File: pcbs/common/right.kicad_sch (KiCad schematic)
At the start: 89 parts, among them J2 TRS

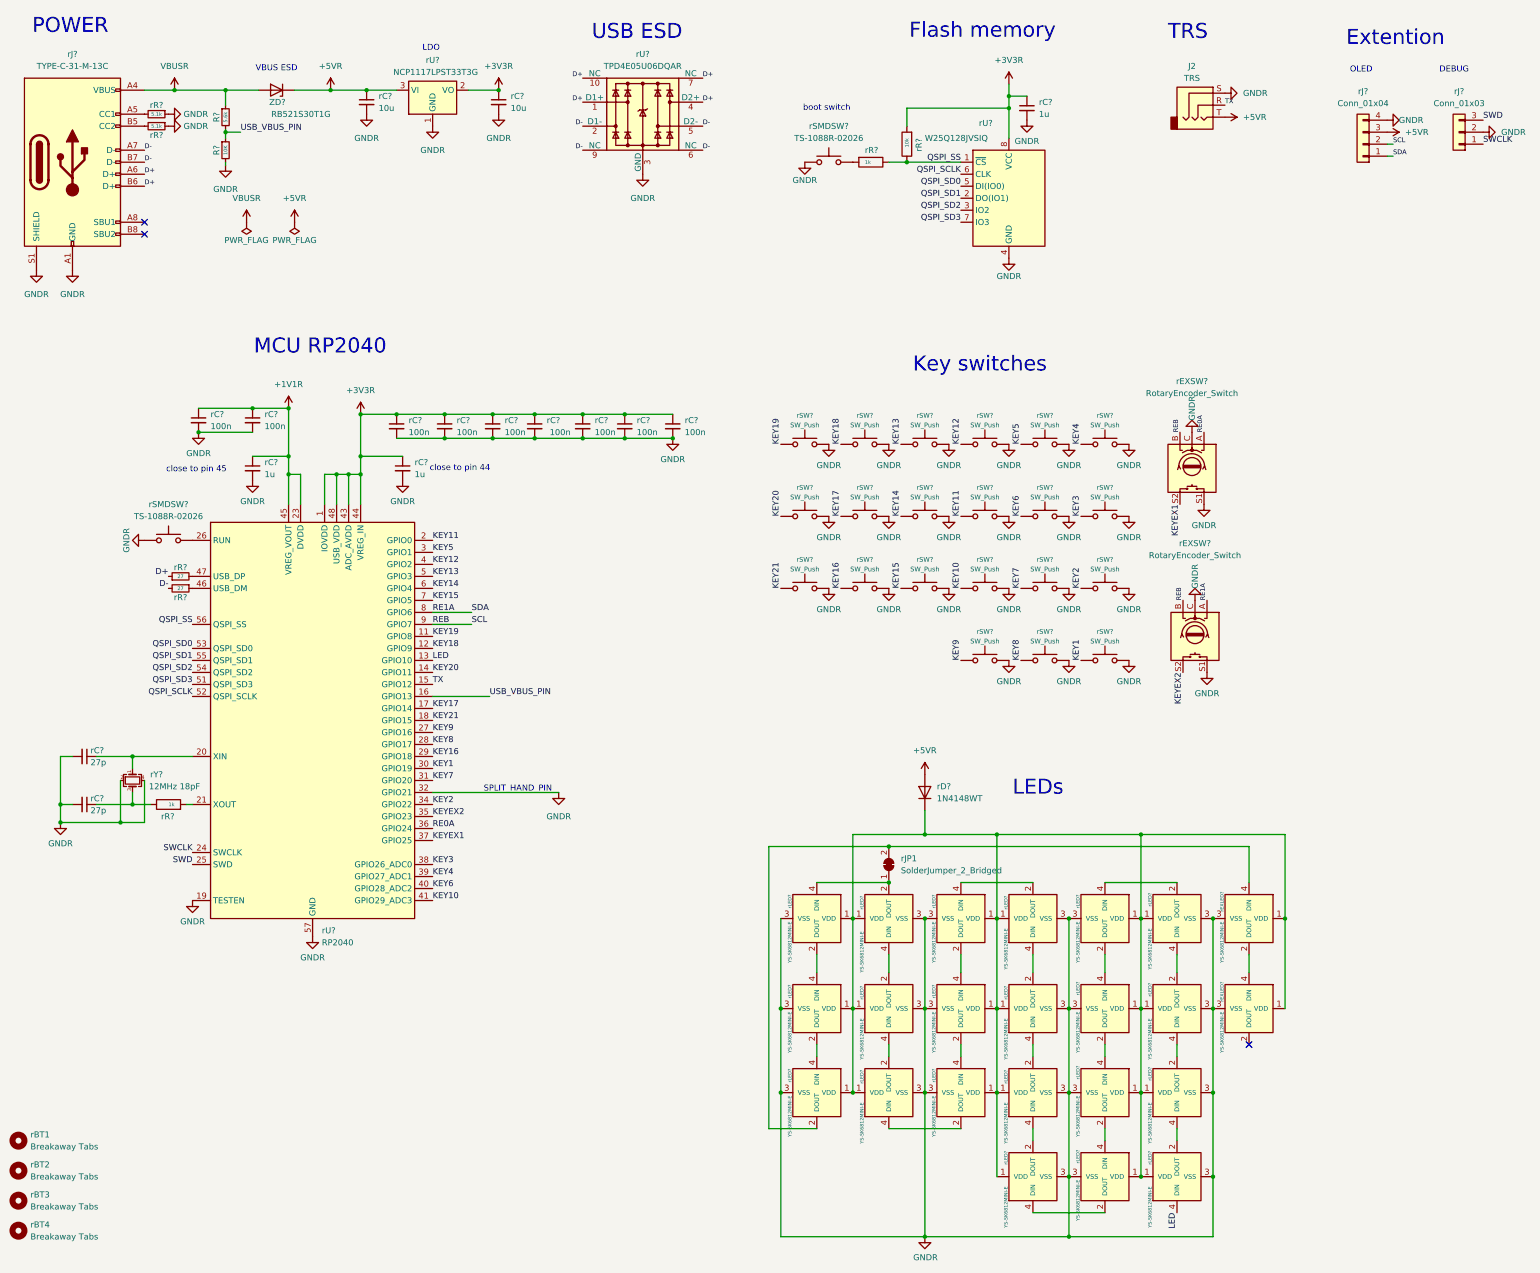
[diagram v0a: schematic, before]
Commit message: KiCad v9
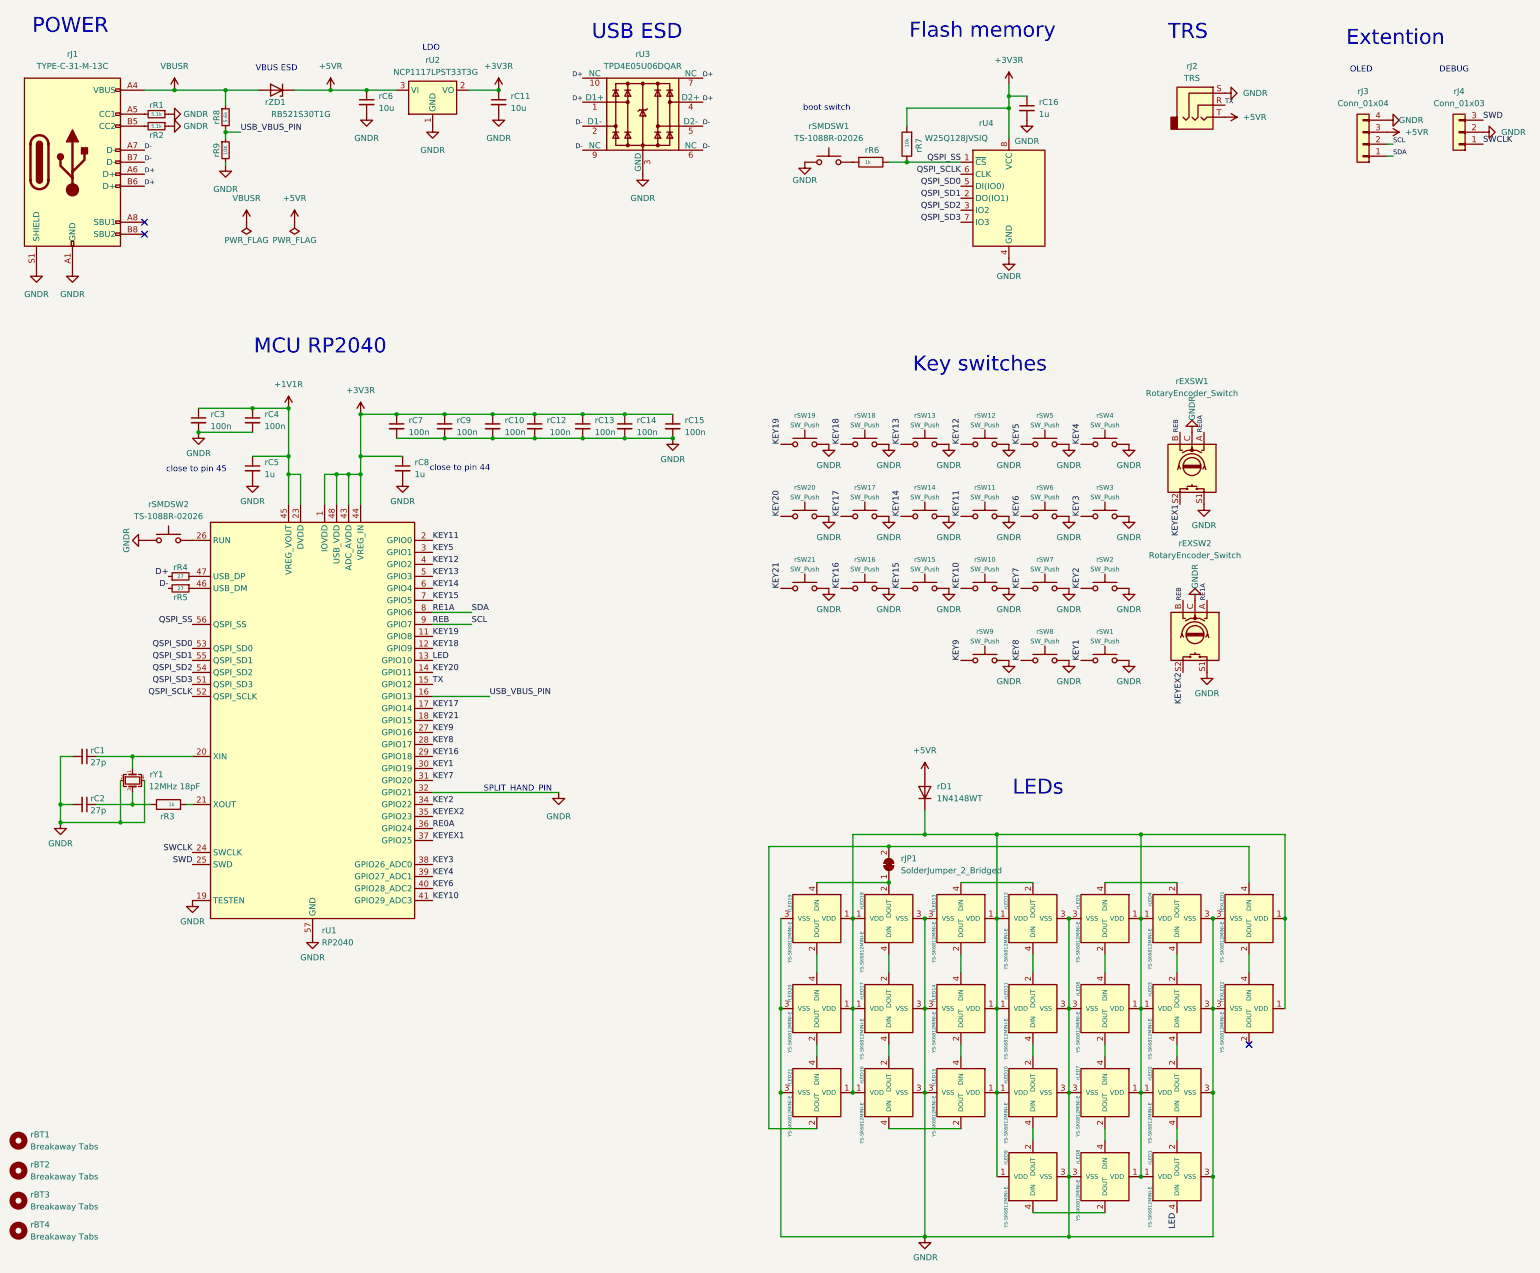
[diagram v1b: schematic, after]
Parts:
- gave numbers to parts that had none: 83
- renumbered J2 to rJ2

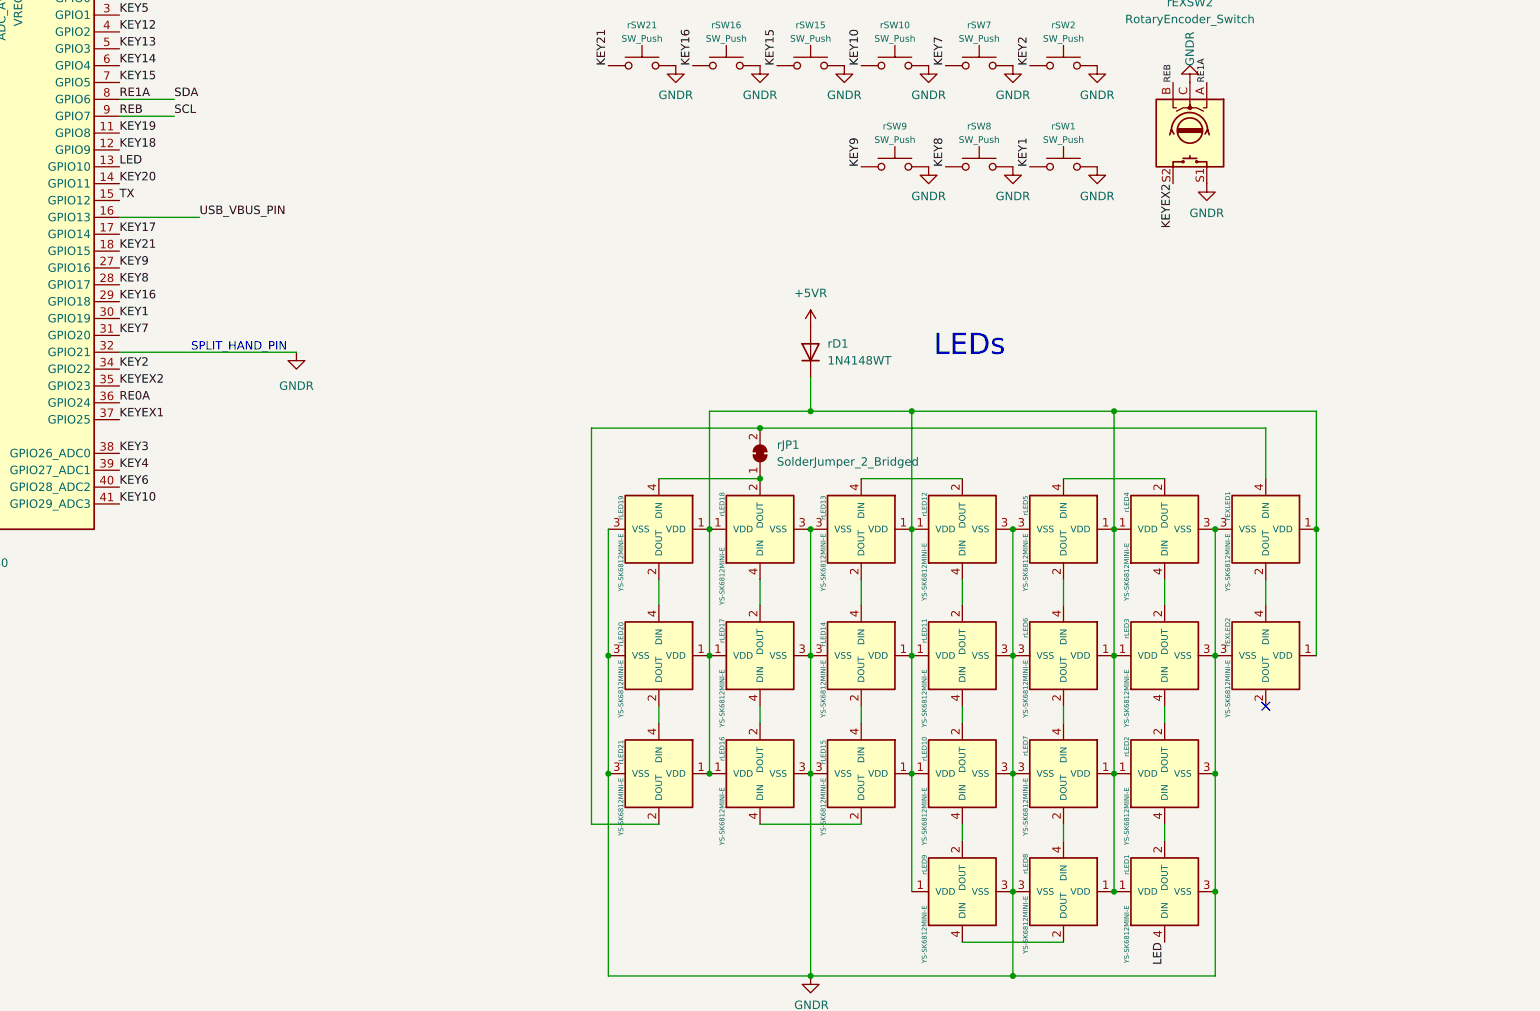
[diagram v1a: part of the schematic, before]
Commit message: add keys and LEDs
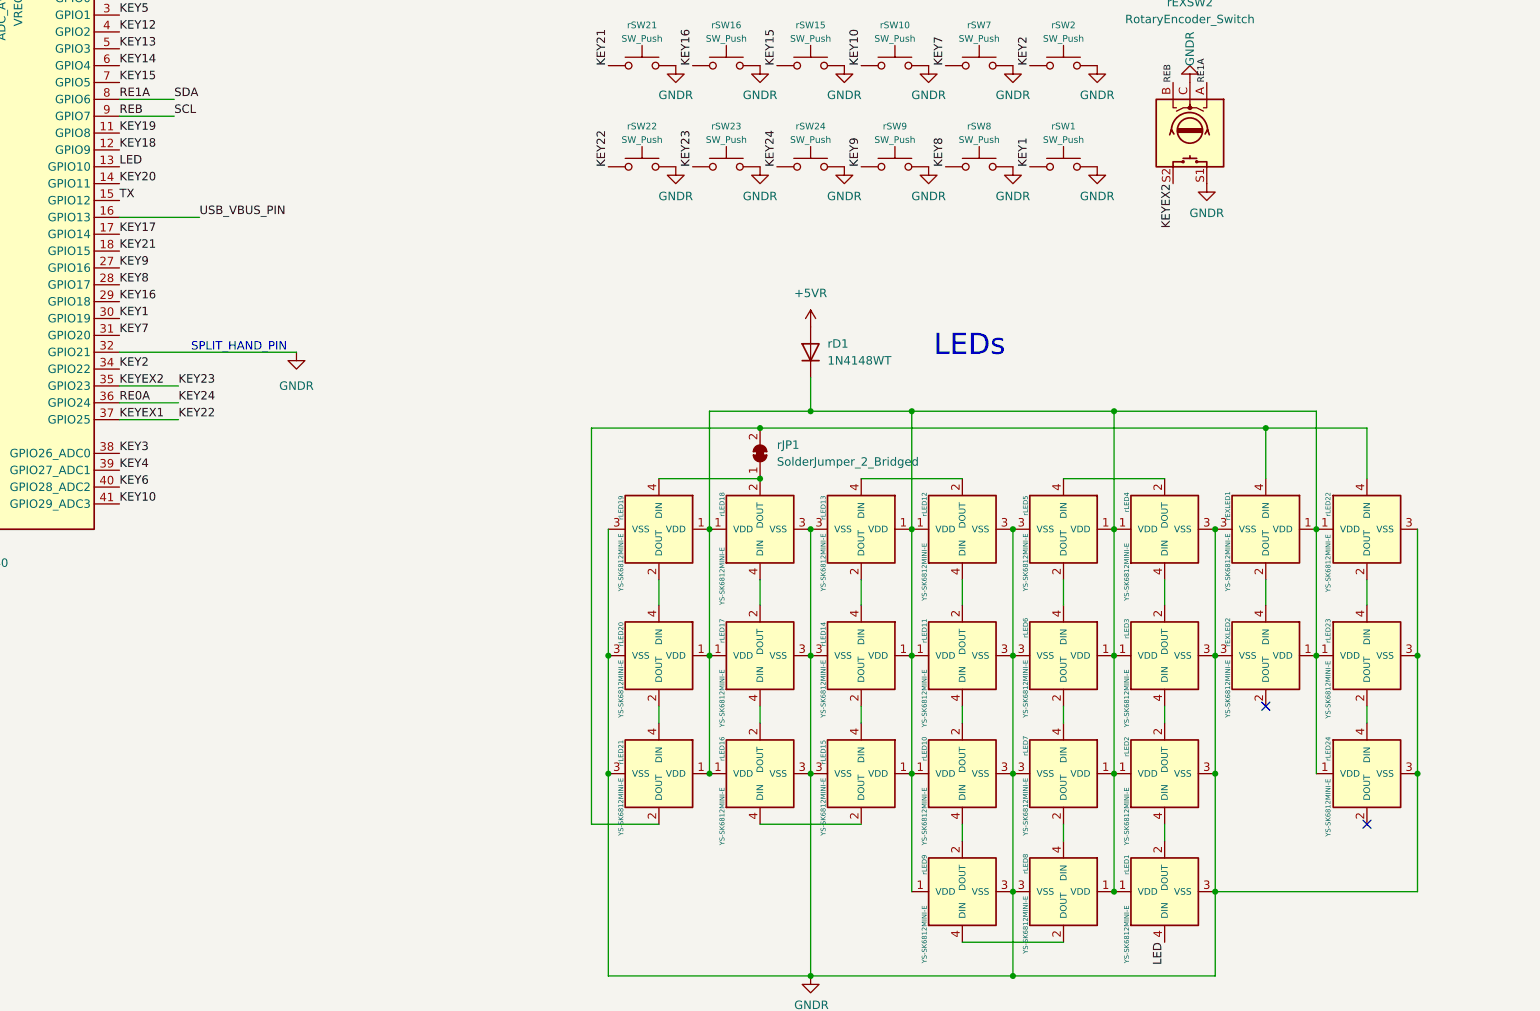
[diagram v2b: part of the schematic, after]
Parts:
- added rLED22, rLED23, rLED24: YS-SK6812MINI-E, kbd_local:YS-SK6812MINI-E, symbol kbd_local:YS-SK6812MINI-E
- added rSW22, rSW23, rSW24: SW_Push, kbd:keyswitch_cherrymx_hotswap_1u, symbol Switch:SW_Push
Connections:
- net GNDR: now also rLED22.3 (VSS), rLED23.3 (VSS), rLED24.3 (VSS), rSW22.2, rSW23.2, rSW24.2
- net at rD1.1 (K), rEXLED1.1 (VDD), rEXLED2.1 (VDD)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: now also rLED22.1 (VDD), rLED23.1 (VDD), rLED24.1 (VDD)
- net at rEXLED1.4 (DIN), rJP1.2 (B), rLED21.2 (DOUT): now also rLED22.4 (DIN)
- net KEYEX1 renamed KEY22
- net KEY22: now also rSW22.1
- net KEYEX2 renamed KEY23
- net KEY23: now also rSW23.1
- net RE0A renamed KEY24
- net KEY24: now also rSW24.1
- new net: rLED23.2 (DOUT), rLED24.4 (DIN)
- new net: rLED22.2 (DOUT), rLED23.4 (DIN)
- no-connect marks 3 -> 4
